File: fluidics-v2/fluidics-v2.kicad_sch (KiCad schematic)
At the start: 32 parts, among them J1 PJ-063AH, J10 87832-1010, J11 0705430001, J12 87832-1010, J13 0705430001, J14 0533980671, J15 87832-1010, J16 0705430001, J17 0533980671, J2 0533980671, J3 A-DS_15_A_KG-T4S, J4 0533980671, J5 1860280, J6 87832-1010, J7 0705430001, J8 87832-1010, J9 0705430001, U2 Teensy4.1, U3 LTC4311CSC6-TRPBF

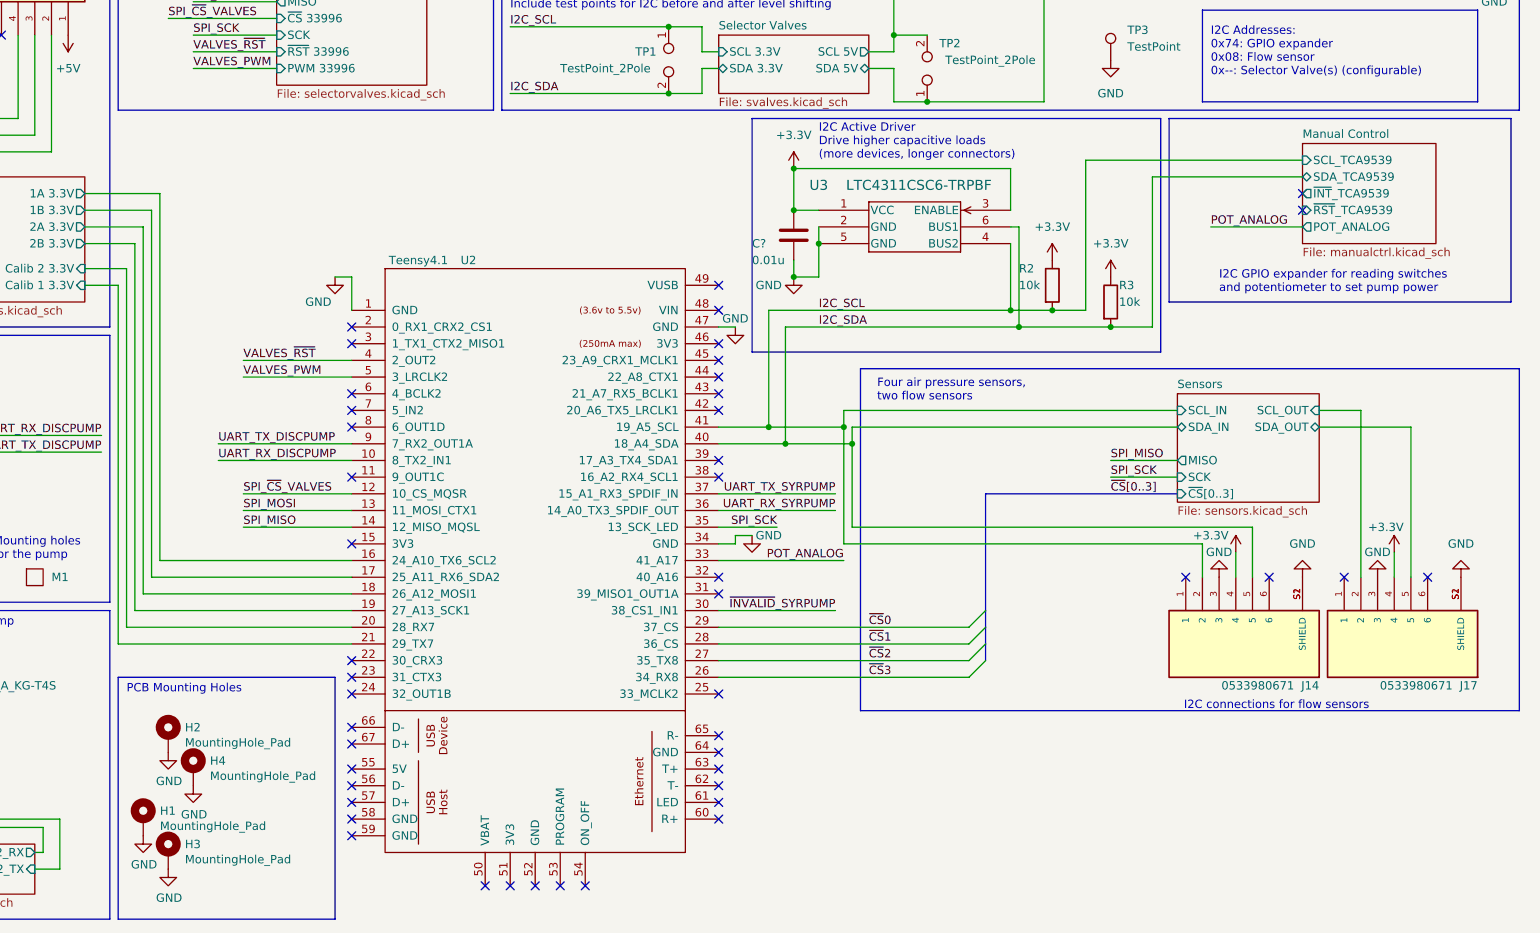
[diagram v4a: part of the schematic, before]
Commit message: added support for more I2C busses (3 + 1 address translator)
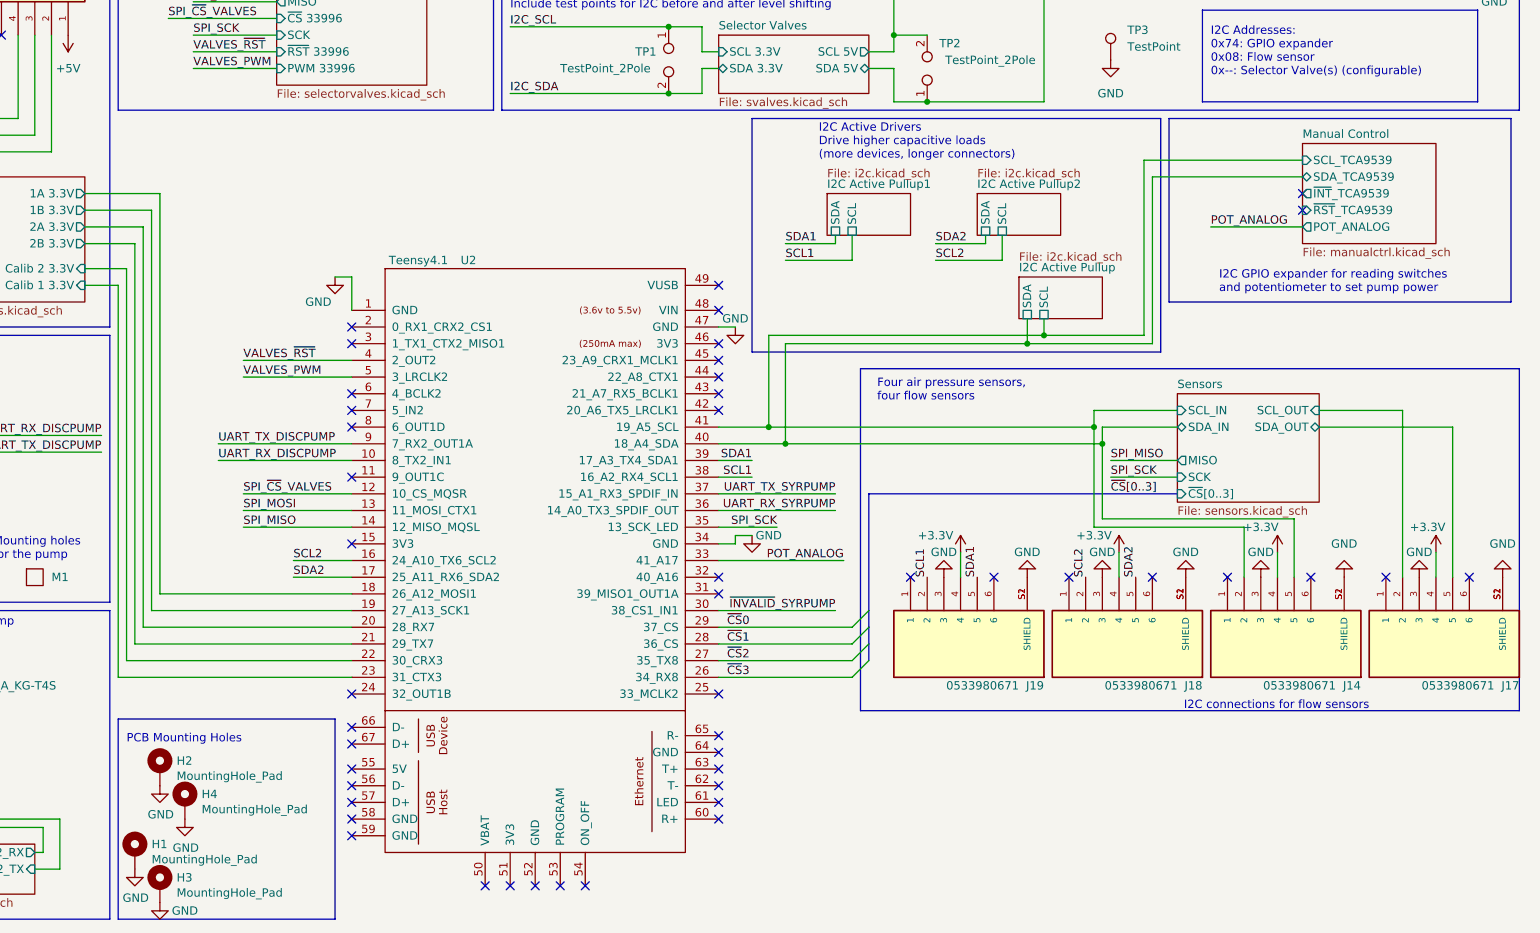
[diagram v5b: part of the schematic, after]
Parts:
- removed C?: 0.01u, Capacitor_SMD:C_0603_1608Metric, symbol Device:C
- removed R2, R3: 10k, Resistor_SMD:R_0402_1005Metric, symbol Device:R
- removed U3: LTC4311CSC6-TRPBF, SOT-6_SC_LIT, symbol LTC4311CSC6#TRPBF:LTC4311CSC6-TRPBF
- added J18, J19: 0533980671, molex_connectors:MOLEX_0533980671, symbol 0533980671:0533980671
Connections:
- net +3.3V: now also J18.4, J19.4
- net Bubble Sensors/1A 3.3V: now also U2.18 (26_A12_MOSI1); no longer U2.16 (24_A10_TX6_SCL2)
- net Bubble Sensors/1B 3.3V: now also U2.19 (27_A13_SCK1); no longer U2.17 (25_A11_RX6_SDA2)
- net Bubble Sensors/2A 3.3V: now also U2.20 (28_RX7); no longer U2.18 (26_A12_MOSI1)
- net Bubble Sensors/2B 3.3V: now also U2.21 (29_TX7); no longer U2.19 (27_A13_SCK1)
- net Bubble Sensors/Calib 1 3.3V: now also U2.23 (31_CTX3); no longer U2.21 (29_TX7)
- net Bubble Sensors/Calib 2 3.3V: now also U2.22 (30_CRX3); no longer U2.20 (28_RX7)
- net GND: now also J18.3, J18.S1 (SHIELD), J18.S2 (SHIELD), J19.3, J19.S1 (SHIELD), J19.S2 (SHIELD)
- net I2C_SCL: no longer J14.2, U2.41 (19_A5_SCL)
- net I2C_SDA: no longer J14.5, U2.40 (18_A4_SDA)
- net SCL1: now reaches U2.38 (16_A2_RX4_SCL1)
- net SCL1: now also J19.2
- net SDA1: now reaches U2.39 (17_A3_TX4_SDA1)
- net SDA1: now also J19.5
- new net I2C Active Pullup/SCL: J14.2, U2.41 (19_A5_SCL)
- new net I2C Active Pullup/SDA: J14.5, U2.40 (18_A4_SDA)
- new net SCL2: J18.2, U2.16 (24_A10_TX6_SCL2)
- new net SDA2: J18.5, U2.17 (25_A11_RX6_SDA2)
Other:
- added sheet I2C Active Pullup (i2c.kicad_sch)
- added sheet I2C Active Pullup1 (i2c.kicad_sch)
- added sheet I2C Active Pullup2 (i2c.kicad_sch)
- note added: "Four air pressure sensors, four flow sensors"
- note added: "I2C Active Drivers Drive higher capacitive loads (more devices, longer connectors)"
- note removed: "Four air pressure sensors, two flow sensors"
- note removed: "I2C Active Driver Drive higher capacitive loads (more devices, longer connectors)"
- moved on the sheet: H1, H2, H3, H4, J14, J17

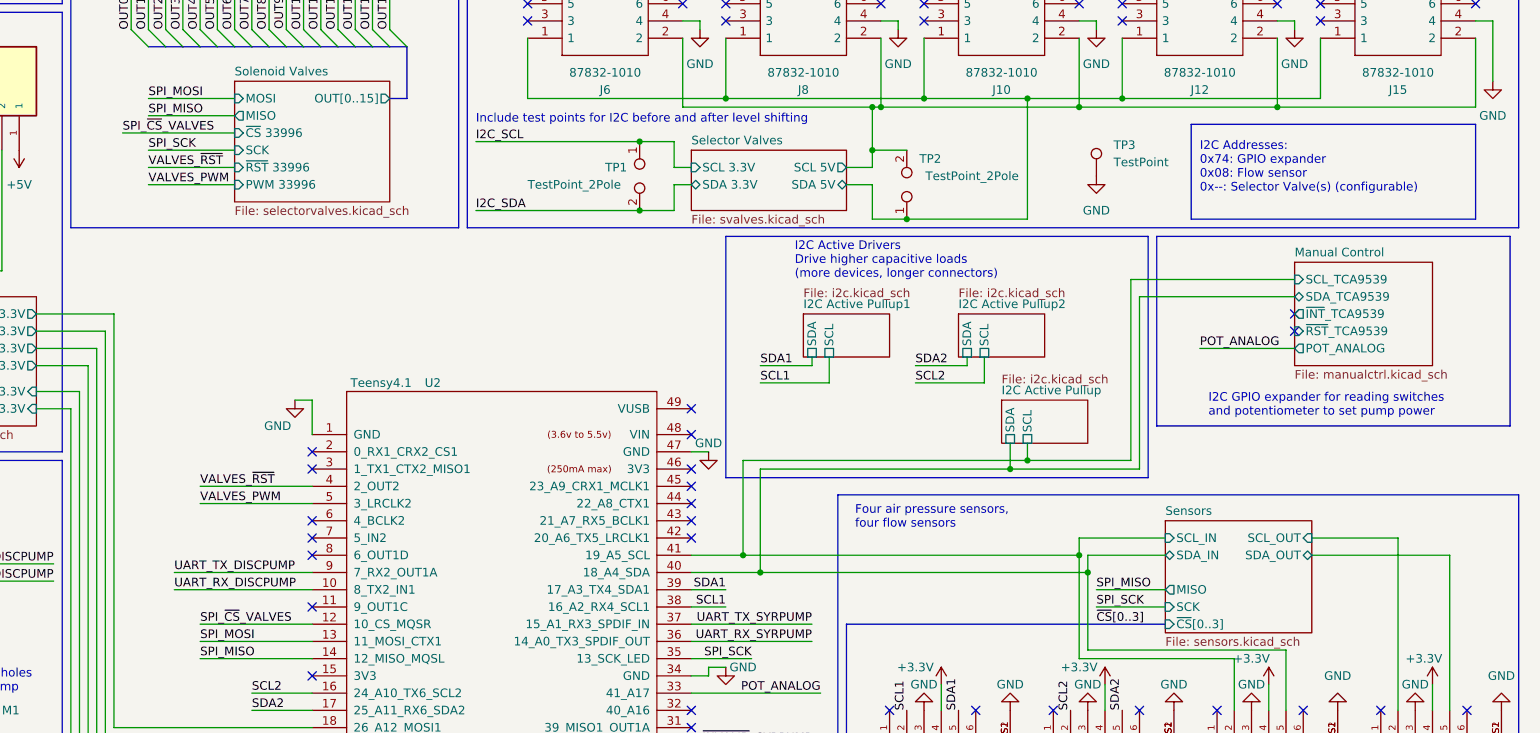
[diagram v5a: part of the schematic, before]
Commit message: added pressure controllers and more flow sensors
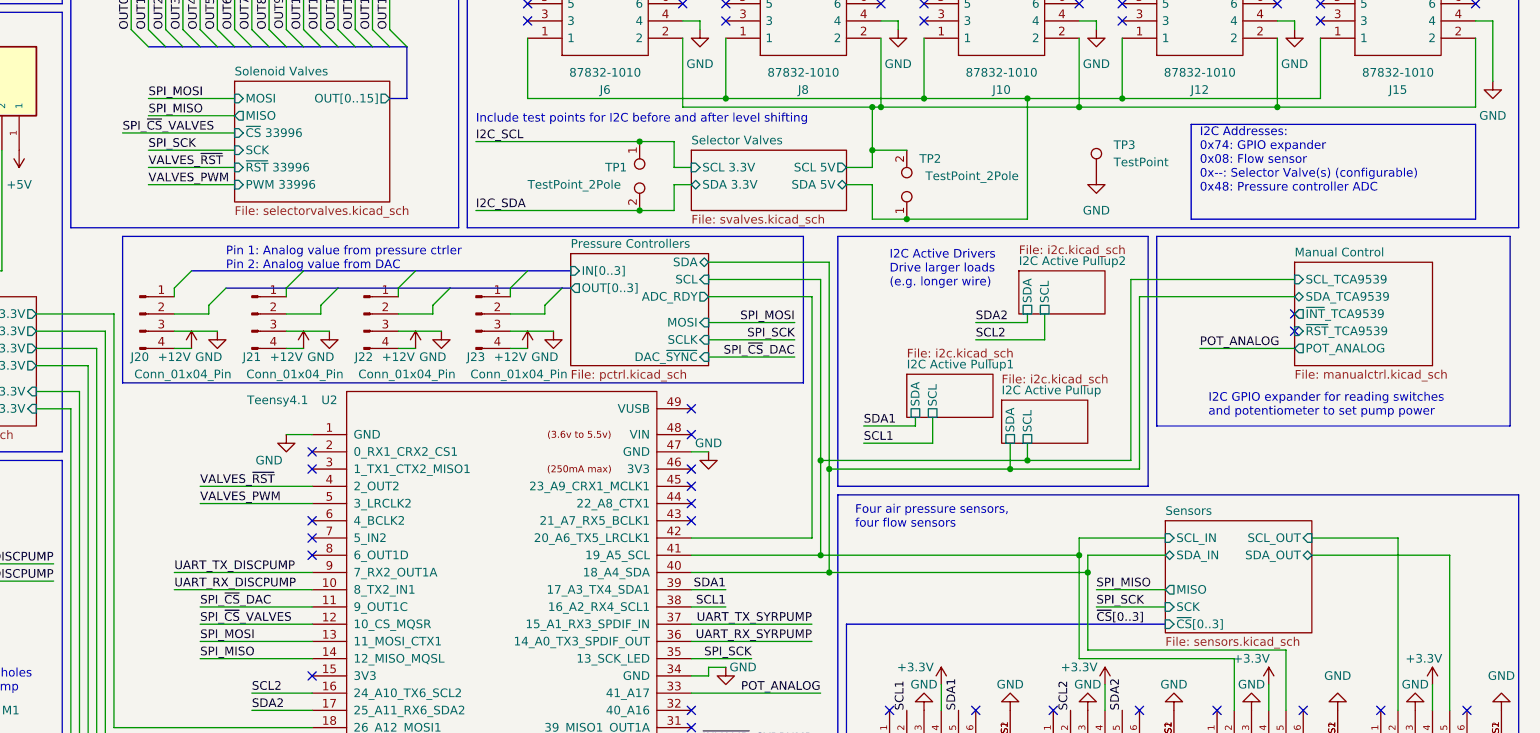
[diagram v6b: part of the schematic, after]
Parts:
- added J20, J21, J22, J23: Conn_01x04_Pin, user-footprints:53047-04, symbol Connector:Conn_01x04_Pin
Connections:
- net +12V: now also J20.4 (Pin_4), J21.4 (Pin_4), J22.4 (Pin_4), J23.4 (Pin_4)
- net GND: now also J20.3 (Pin_3), J21.3 (Pin_3), J22.3 (Pin_3), J23.3 (Pin_3)
- net SPI_~{CS}_DAC: now reaches U2.11 (9_OUT1C)
- net Pressure Controllers/ADC_RDY: now reaches U2.42 (20_A6_TX5_LRCLK1)
- no-connect marks 106 -> 104
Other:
- added sheet Pressure Controllers (pctrl.kicad_sch)
- note added: "I2C Active Drivers Drive larger loads (e.g. longer wire)"
- note added: "I2C Addresses: 0x74: GPIO expander 0x08: Flow sensor 0x--: Selector Valve(s) (configurable) 0x48: Pressure controller ADC"
- note added: "Pin 1: Analog value from pressure ctrler Pin 2: Analog value from DAC"
- note removed: "I2C Active Drivers Drive higher capacitive loads (more devices, longer connectors)"
- note removed: "I2C Addresses: 0x74: GPIO expander 0x08: Flow sensor 0x--: Selector Valve(s) (configurable)"

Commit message: added new connector for motor control daughter board. began layout
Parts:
- removed J20, J21, J22, J23: Conn_01x04_Pin, user-footprints:53047-04, symbol Connector:Conn_01x04_Pin
- added D21: B340-13-F, Diode_SMD:D_SMC, symbol Device:D
- added J6: Conn_02x14_Counter_Clockwise, Package_DIP:DIP-28_W15.24mm_Socket, symbol Connector_Generic:Conn_02x14_Counter_Clockwise
- added J7: Conn_02x03_Odd_Even, Connector_PinHeader_2.54mm:PinHeader_2x03_P2.54mm_Vertical, symbol Connector_Generic:Conn_02x03_Odd_Even
- added J8: 5031542690, 5031492600:CON_5031542690, symbol 5031492600:5031542690
- added JP3: SolderJumper_2_Bridged, Jumper:SolderJumper-2_P1.3mm_Bridged_Pad1.0x1.5mm, symbol Jumper:SolderJumper_2_Bridged
- renumbered J6 to J10, J7 to J11, J8 to J12, J9 to J13, J10 to J14, J19 to J15, J11 to J16, J18 to J17, J12 to J18, J13 to J19, J14 to J20, J15 to J21, J16 to J22, J17 to J23
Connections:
- net +12V: now also J6.14 (Pin_14), J8.7, J8.8; no longer J1.1
- net +24V: now also J1.1, J8.5, J8.6
- net +3.3V: now also J8.10, JP3.1 (A)
- net +5V: now also D21.2 (A), J6.17 (Pin_17), J8.9
- net GND: now also J6.13 (Pin_13), J6.23 (Pin_23), J8.1, J8.2, J8.27, J8.28, J8.3, J8.4
- net SCL1: now also J8.23
- net SCL2: now also J8.21
- net SDA1: now also J8.24
- net SDA2: now also J8.22
- net SPI_MISO: now also J6.28 (Pin_28), J8.19
- net SPI_MOSI: now also J6.27 (Pin_27), J8.20
- net SPI_SCK: now also J6.26 (Pin_26), J8.18
- net GPIO_6: now reaches U2.25 (33_MCLK2)
- net GPIO_6: now also J8.11
- net GPIO_5: now reaches U2.32 (40_A16)
- net GPIO_5: now also J8.12
- net GPIO_3: now reaches U2.43 (21_A7_RX5_BCLK1)
- net GPIO_3: now also J8.14
- net GPIO_2: now reaches U2.44 (22_A8_CTX1)
- net GPIO_2: now also J8.15
- net GPIO_1: now reaches U2.45 (23_A9_CRX1_MCLK1)
- net GPIO_1: now also J8.16
- net GPIO_0: now reaches U2.46 (3V3)
- net GPIO_0: now also J8.17
- net at U2.48 (VIN): now also D21.1 (K)
- net Power Supplies/PG-12V: now reaches U2.7 (5_IN2)
- net Power Supplies/PG-5V: now reaches U2.8 (6_OUT1D)
- net I2C Active Pullup/SCL renamed SDA
- net SDA: now also J8.26
- net I2C Active Pullup/SDA renamed SCL
- net SCL: now also J8.25
- net Pressure Controllers/ADC_RDY renamed GPIO_4
- net GPIO_4: now also J8.13
- net SPI_~{CS}_DAC renamed SPI_~{CS}_PRESS
- net SPI_~{CS}_PRESS: now also J6.25 (Pin_25)
- new net: J6.2 (Pin_2), J6.24 (Pin_24), J7.2 (Pin_2), JP3.2 (B)
- new net: J6.1 (Pin_1), J7.5 (Pin_5)
- new net: J6.3 (Pin_3), J7.6 (Pin_6)
- new net: J6.4 (Pin_4), J7.4 (Pin_4)
- new net: J6.5 (Pin_5), J7.3 (Pin_3)
- no-connect marks 104 -> 109
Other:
- removed sheet Pressure Controllers
- sheet Power Supplies ports: added PG-12V, PG-5V; removed none
- note added: "Connection to daughter board Wire - Wire3 (6 wires) 3.3V 5V 12V 24V SPI (3 wires) GPIO (7 wires)"
- note added: "Convert from 24V to: - 12V - 5V - 3.3V"
- note added: "ICSP"
- note added: "Note: Cut the jumper when using the ICSP header and bridge it when done. Pressure controller module from Wenzel lab"
- note removed: "Convert from 12V to: - 24V - 5V - 3.3V"
- note removed: "Pin 1: Analog value from pressure ctrler Pin 2: Analog value from DAC"
- moved on the sheet: H1, H2, H3, H4, J1, J10, J11, J12, J13, J14, J15, J16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

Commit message: done w/ layout
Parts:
- removed J8: 5031542690, 5031492600:CON_5031542690, symbol 5031492600:5031542690
- added J8: 5031543090, 5031543090:CON_5031543090, symbol 5031543090:5031543090
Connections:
- net +12V: now also J8.8, J8.9
- net +24V: now also J8.5, J8.6, J8.7
- net +3.3V: now also J8.11
- net +5V: now also J8.10
- net GND: now also J8.1, J8.2, J8.3, J8.31, J8.32, J8.4
- net GPIO_0: now also J8.21
- net GPIO_1: now also J8.20
- net GPIO_2: now also J8.19
- net GPIO_3: now also J8.18
- net GPIO_4: now also J8.17
- net GPIO_5: now also J8.16
- net GPIO_6: now also U2.31 (39_MISO1_OUT1A), J8.15; no longer U2.25 (33_MCLK2)
- net SCL: now also J8.29
- net SCL1: now also J8.27
- net SCL2: now also J8.25
- net SDA: now also J8.30
- net SDA1: now also J8.28
- net SDA2: now also J8.26
- net SPI_MISO: now also J8.23
- net SPI_MOSI: now also J8.24
- net SPI_SCK: now also J8.22
- net GPIO_8: now reaches U2.24 (32_OUT1B)
- net GPIO_8: now also J8.13
- net GPIO_9: now reaches U2.6 (4_BCLK2)
- net GPIO_9: now also J8.12
- new net GPIO_7: J8.14, U2.25 (33_MCLK2)
- no-connect marks 109 -> 107
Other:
- note added: "Connection to daughter board I2C 0 - I2C 2 (6 wires) 3.3V 5V 12V 24V SPI (3 wires) GPIO (10 wires)"
- note removed: "Connection to daughter board Wire - Wire3 (6 wires) 3.3V 5V 12V 24V SPI (3 wires) GPIO (7 wires)"
